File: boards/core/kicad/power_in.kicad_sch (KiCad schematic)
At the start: 31 parts, among them J1 USB4105-GF-A-120, Q1 AO4485, Q2 2N7002, Q3 S8050, U1 CH224Q, U2 USBLC6-2SC6, U3 INA186A1

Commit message: The boards will work on the first spin: independent engineering reviews of Lite and core, fixes and contingencies built…
* First-spin review: the brief each domain reviewer works from

* First-spin review: partial drafts saved before the reviewers' login d…

…ropped

* First-spin review: power, audio, digital and thermal reviews of lite-…

…main and core, with their sims

* core carries its EasyEDA CPL model cache, so its dfm gate runs withou…

…t EasyEDA (red on 403 otherwise); DFM review

* First-spin review: parts pin-to-pad audit of both boards

* Lite board after the first-spin review: amp SDZ, PVDD switch hold-off…

… and soft start, line-in headroom, 5 V loop, RCA slots, HRO USB-C and CH340B, speaker loopback taps; regenerated on hwde c23e27e, all gates pass

Review-2 findings fixed on lite-main as an ECO on the routed board (no
re-route): AUDIO-4/DIGITAL-14, POWER-3/4/10, AUDIO-7, DFM-2, stock swaps.
Also: the speaker loopback taps (task 261029-033806) and the hwde refresh
(task 261029-004401) for this board. Known-unknowns list and its order-step
check (tools/known_unknowns.py). Unit cost at 100: 13.16 (was 13.05).

* core (Plus/Ultra) after the first-spin review: TCA9539 with ESP32 res…

…et, 5 A path via patches and through-hole USB4085, antenna keep-out, PVDD switch SOA and PD-PG gating, OPA1678 headroom, RCA and TOSLINK holes, front IR, 49.152 MHz DAC clock, speaker loopback taps; all gates pass

Review-2 blockers fixed on core: DIGITAL-1/2/PARTS-4, POWER-1, DFM-1, PARTS-7;
THERMAL-1 handled by a lid-pressed heatsink plus firmware governor (no room
for clip holes). Majors: POWER-2/6, AUDIO-1/2/3, DIGITAL-19, DFM-4. Done as an
ECO on the routed board; Ultra zone-B taps left out (no control line).

* First-spin review: every finding's disposition, known-unknowns resolv…

…ed for Lite and Plus (order gate by tier), firmware duties for core, R45 2.2k, honest TPA3221 thermal constraint, Plus/Ultra cost estimate

* Heatsink options for the TPA3221 checked aga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
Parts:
- added R20: 10k, aiee:R0402, symbol Device:R
- C8: value 1uF -> 2.2uF; LCSC C28323 -> C377773
- J1: value USB4105-GF-A-120 -> USB4085-GF-A; footprint aiee:USB-C-SMD_MC-311D -> aiee:USC-C-SMD_USB4085-GF-A; symbol aiee:USB4105-GF-A-120 -> aiee:USB4085-GF-A_C7095263; LCSC C5184243 -> C7095263; MPN (none) -> USB4085-GF-A
- R4, R5: value 100k -> 470k; LCSC C25741 -> C25790
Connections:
- net +3V3: now also R20.1
- net CC1: now also U1.6 (CC2); no longer U1.7 (CC1)
- net CC2: now also U1.7 (CC1); no longer U1.6 (CC2)
- net GND: now also J1.A1 (GND), J1.A12 (GND), J1.B1 (GND), J1.B12 (GND), J1.S1; no longer J1.1 (EH), J1.2 (EH), J1.3 (EH), J1.4 (EH), J1.A1-B12 (GND), J1.B1-A12 (GND), Q2.2 (S), U1.10 (PG)
- net VBUS_IN: now also J1.A4 (VBUS), J1.A9 (VBUS), J1.B4 (VBUS), J1.B9 (VBUS); no longer J1.A4-B9 (VBUS), J1.B4-A9 (VBUS)
- new net PD_PG: Q2.2 (S), R20.2, U1.10 (PG)
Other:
- moved on the sheet: C1, C2, C3, C4, C5, C6, C7, C8, C9, Q1, Q2, Q3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

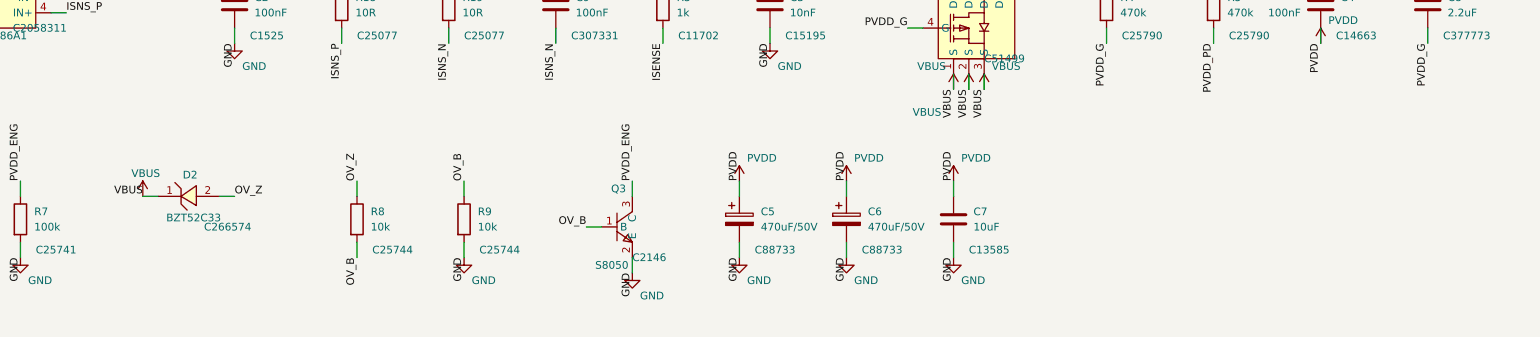
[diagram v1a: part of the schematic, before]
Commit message: TPA3221 heatsink the person doesn't have to fit: a JLC-fittable board-mount part or a pad-down amp
* First-spin review: the brief each domain reviewer works from

* First-spin review: partial drafts saved before the reviewers' login d…

…ropped

* First-spin review: power, audio, digital and thermal reviews of lite-…

…main and core, with their sims

* core carries its EasyEDA CPL model cache, so its dfm gate runs withou…

…t EasyEDA (red on 403 otherwise); DFM review

* First-spin review: parts pin-to-pad audit of both boards

* Lite board after the first-spin review: amp SDZ, PVDD switch hold-off…

… and soft start, line-in headroom, 5 V loop, RCA slots, HRO USB-C and CH340B, speaker loopback taps; regenerated on hwde c23e27e, all gates pass

Review-2 findings fixed on lite-main as an ECO on the routed board (no
re-route): AUDIO-4/DIGITAL-14, POWER-3/4/10, AUDIO-7, DFM-2, stock swaps.
Also: the speaker loopback taps (task 261029-033806) and the hwde refresh
(task 261029-004401) for this board. Known-unknowns list and its order-step
check (tools/known_unknowns.py). Unit cost at 100: 13.16 (was 13.05).

* core (Plus/Ultra) after the first-spin review: TCA9539 with ESP32 res…

…et, 5 A path via patches and through-hole USB4085, antenna keep-out, PVDD switch SOA and PD-PG gating, OPA1678 headroom, RCA and TOSLINK holes, front IR, 49.152 MHz DAC clock, speaker loopback taps; all gates pass

Review-2 blockers fixed on core: DIGITAL-1/2/PARTS-4, POWER-1, DFM-1, PARTS-7;
THERMAL-1 handled by a lid-pressed heatsink plus firmware governor (no room
for clip holes). Majors: POWER-2/6, AUDIO-1/2/3, DIGITAL-19, DFM-4. Done as an
ECO on the routed board; Ultra zone-B taps left out (no control line).

* First-spin review: every finding's disposition, known-unknowns resolv…

…ed for Lite and Plus (order gate by tier), firmware duties for core, R45 2.2k, honest TPA3221 thermal constraint, Plus/Ultra cost estimate

* Heatsink options for the TPA3221 checked against the lead's order;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
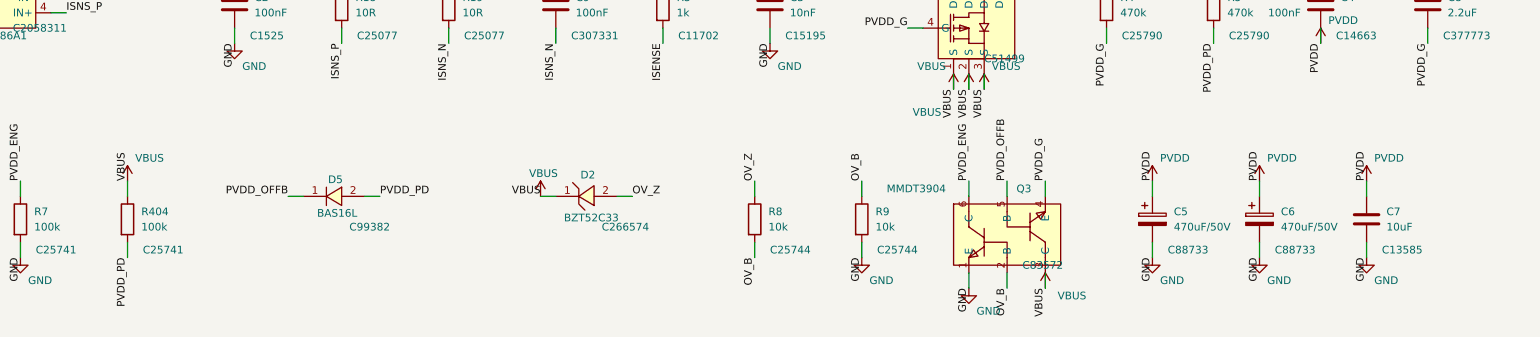
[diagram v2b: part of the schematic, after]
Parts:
- added D5: BAS16L, aiee:SOD-882_L1.0-W0.6-RD, symbol aiee:BAS16L,315
- added R404: 100k, aiee:R0402, symbol Device:R
- Q3: value S8050 -> MMDT3904; footprint aiee:SOT-23-3_L3.0-W1.7-P0.95-LS2.9-BR -> aiee:SOT-363_L2.0-W1.3-P0.65-LS2.1-TL; symbol aiee:S8050_C2146 -> aiee:MMDT3904-7-F; LCSC C2146 -> C83572
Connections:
- net GND: now also Q3.1 (E); no longer Q3.2 (E)
- net OV_B: now also Q3.2 (B); no longer Q3.1 (B)
- net PVDD_ENG: now also Q3.6 (C); no longer Q3.3 (C)
- net PVDD_G: now also Q3.4 (E)
- net PVDD_PD: now also D5.2 (A), R404.2
- net VBUS: now also Q3.3 (C), R404.1
- new net PVDD_OFFB: D5.1 (K), Q3.5 (B)
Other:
- moved on the sheet: C5, C6, C7, D2, R8, R9
